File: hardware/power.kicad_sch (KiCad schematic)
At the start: 33 parts, among them Q6 Q_PMOS_GDS

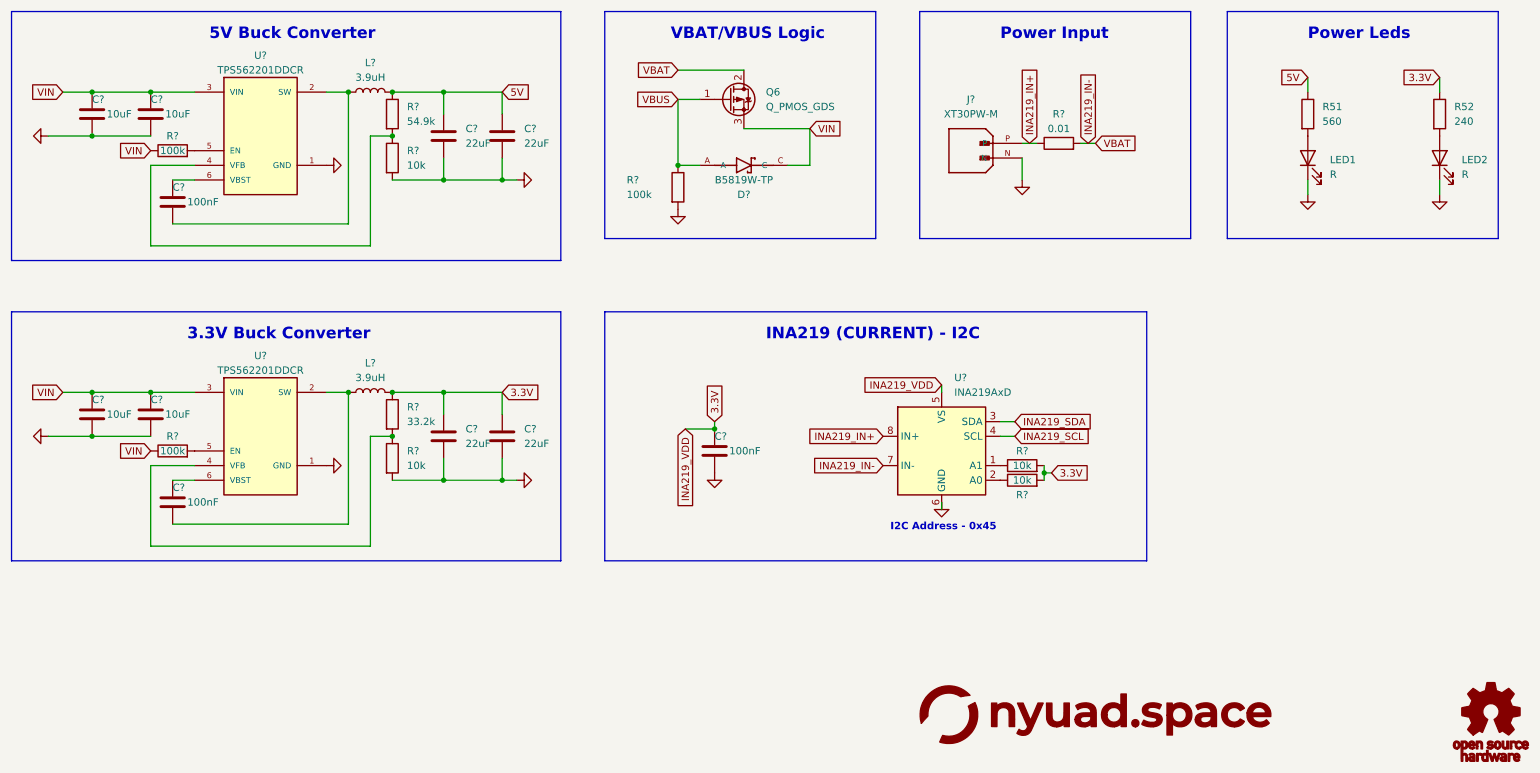
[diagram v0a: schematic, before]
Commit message: added BNO086
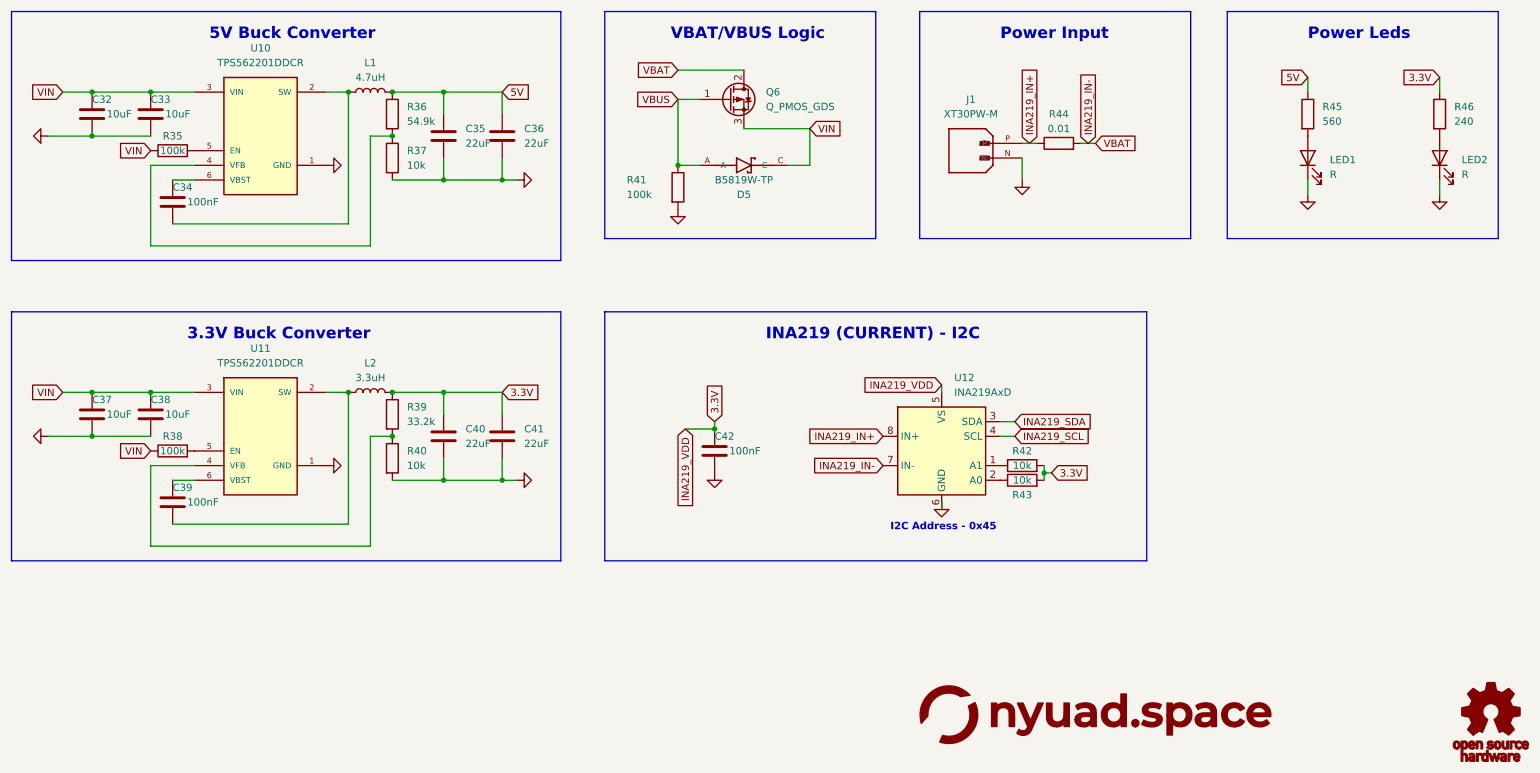
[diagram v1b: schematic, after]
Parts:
- C32, C33, C37, C38: renamed from C?; footprint Capacitor_SMD:C_0603_1608Metric -> (none)
- C35, C36, C40, C41: renamed from C?; footprint Capacitor_SMD:C_0805_2012Metric -> (none)
- C39, C42: renamed from C?; footprint Capacitor_SMD:C_0402_1005Metric -> (none)
- D5: renamed from D?; footprint SOD3716X135N -> (none)
- J1: renamed from J?; footprint Connector_AMASS:AMASS_XT30PW-M_1x02_P2.50mm_Horizontal -> (none)
- L1: renamed from L?; value 3.9uH -> 4.7uH; footprint Inductor_SMD:L_0603_1608Metric -> (none)
- L2: renamed from L?; value 3.9uH -> 3.3uH; footprint Inductor_SMD:L_0603_1608Metric -> (none)
- LED1, LED2: footprint LED_SMD:LED_0603_1608Metric -> (none)
- Q6: footprint Package_TO_SOT_SMD:SOT-23 -> (none)
- R35, R36, R37, R38, R39, R40, R41: renamed from R?; footprint Resistor_SMD:R_0603_1608Metric -> (none)
- R42, R43: renamed from R?; footprint Resistor_SMD:R_0402_1005Metric -> (none)
- R44: renamed from R?; footprint Resistor_SMD:R_2512_6332Metric -> (none)
- R45: renamed from R51; footprint Resistor_SMD:R_0603_1608Metric -> (none)
- R46: renamed from R52; footprint Resistor_SMD:R_0603_1608Metric -> (none)
- U10, U11: renamed from U?; footprint SOT95P280X110-6N -> (none)
- U12: renamed from U?; footprint Package_SO:SOIC-8_3.9x4.9mm_P1.27mm -> (none)
- gave numbers to parts that had none: 1

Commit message: rev2 component placement
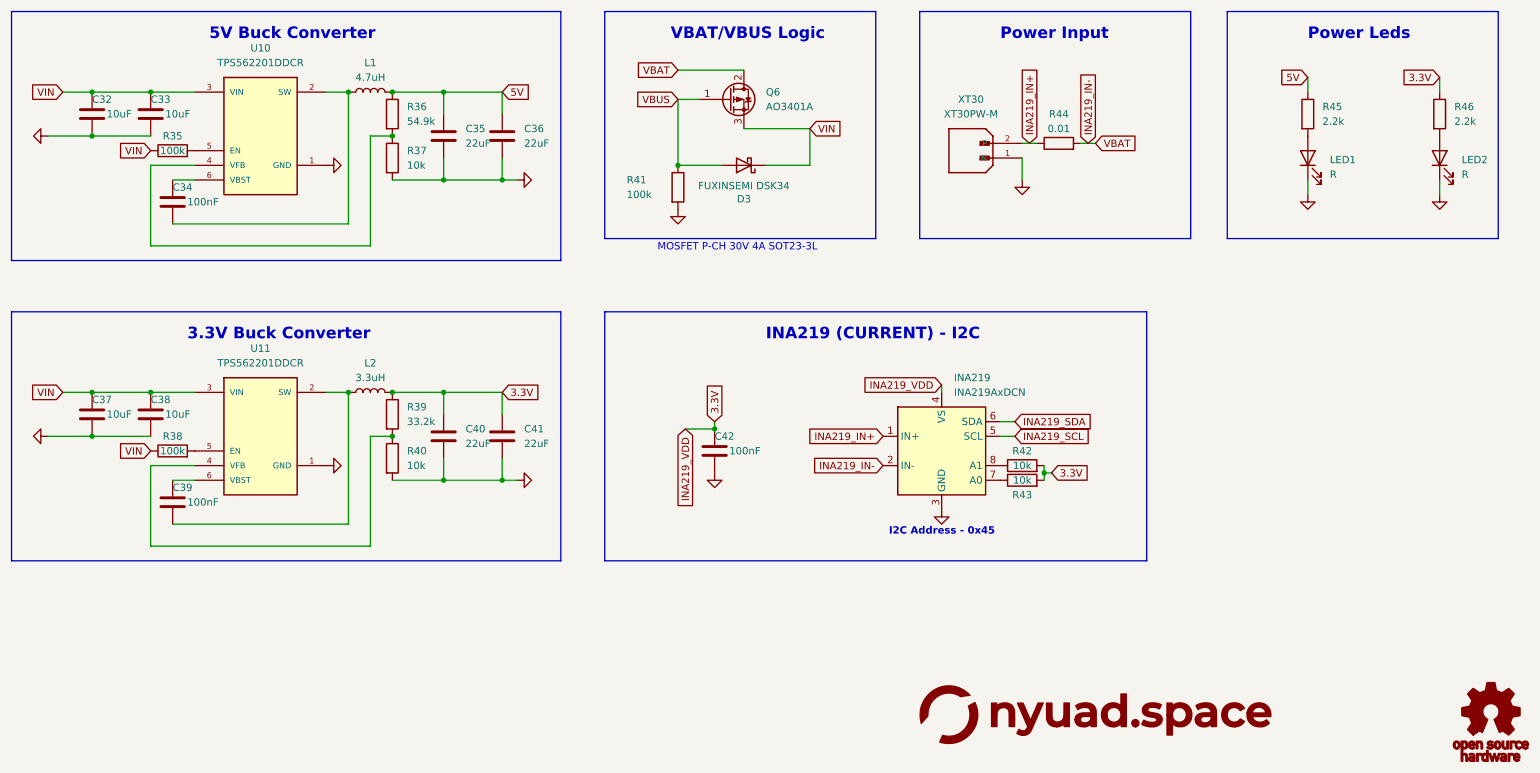
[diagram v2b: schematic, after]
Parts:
- removed D5: B5819W-TP, symbol B5819W-TP:B5819W-TP
- removed U12: INA219AxD, symbol Sensor_Energy:INA219AxD
- added D3: FUXINSEMI DSK34, Diode_SMD:D_SOD-123, symbol Device:D_Schottky
- added INA219: INA219AxDCN, Package_TO_SOT_SMD:SOT-23-8, symbol Sensor_Energy:INA219AxDCN
- C32, C33, C35, C36, C37, C38, C40, C41: footprint (none) -> Capacitor_SMD:C_0805_2012Metric
- C39, C42: footprint (none) -> Capacitor_SMD:C_0402_1005Metric
- L1: footprint (none) -> Inductor_SMD:L_Changjiang_FXL0420
- L2: footprint (none) -> Inductor_SMD:L_Changjiang_FNR4030S
- LED1, LED2: footprint (none) -> LED_SMD:LED_0603_1608Metric
- Q6: value Q_PMOS_GDS -> AO3401A; footprint (none) -> Package_TO_SOT_SMD:SOT-23
- R35, R38, R41: footprint (none) -> Resistor_SMD:R_0603_1608Metric
- R36, R37, R39, R40, R42, R43: footprint (none) -> Resistor_SMD:R_0402_1005Metric
- R44: footprint (none) -> Resistor_SMD:R_2512_6332Metric
- R45: value 560 -> 2.2k; footprint (none) -> Resistor_SMD:R_0603_1608Metric
- R46: value 240 -> 2.2k; footprint (none) -> Resistor_SMD:R_0603_1608Metric
- U10, U11: footprint (none) -> Package_TO_SOT_SMD:TSOT-23-6_HandSoldering
- XT30: renamed from J1; footprint (none) -> Connector_AMASS:AMASS_XT30PW-M_1x02_P2.50mm_Horizontal
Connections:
- net 3.3V: now also INA219.4 (VS)
- net GND: now also XT30.1 (N), INA219.3 (GND); no longer XT30.N
- net INA219_IN+: now also XT30.2 (P), INA219.1 (IN+); no longer XT30.P
- net INA219_IN-: now also INA219.2 (IN-)
- net INA219_SCL: now also INA219.5 (SCL)
- net INA219_SDA: now also INA219.6 (SDA)
- net VBUS: now also D3.2 (A)
- net VIN: now also D3.1 (K)
- net at R42.1: now also INA219.8 (A1)
- net at R43.1: now also INA219.7 (A0)
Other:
- note added: "MOSFET P-CH 30V 4A SOT23-3L"
